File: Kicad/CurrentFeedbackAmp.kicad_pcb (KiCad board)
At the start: 2 copper layers, 200 x 100 mm, 123 parts, among them J1 Test_Etapa_3_Inf, J10 Protecc_Sup_In1, J11 Protecc_Inf_In1, J12 Protecc_Sup_In2, J13 Test_Etapa_3_Inf, J14 Entrada, J15 Salida masa2, J16 Salida tierra, J17 Salida senal, J2 Test_Realim_Out, J3 Salida masa1, J4 Protecc_Sup_Out, J5 Protecc_Inf_Out, J6 Conector Vcc, J7 Conector Vdd, J8 Test_Etapa_3_Inf, J9 Test_Etapa_3_Sup, Q1 TIP42C, Q10 BC858, Q11 BC848, Q12 BC858, Q13 BC559, Q14 BC559, Q15 BC559, Q16 BC549, Q17 BC549, Q18 BC549, Q19 BC559, Q2 BD135, Q20 BC549, Q21 BC559, Q22 BC549, Q23 BC848, Q24 BD136, Q25 BC858, Q26 BC848, Q27 BC848, Q28 BC848, Q29 BC858, Q3 BD136, Q30 BC858, Q31 BC848, Q32 BC858, Q33 BD135, Q34 TIP41C, Q35 BC858, Q36 BC848, Q37 BC848, Q38 BC848, Q4 BC848, Q40 BC858, Q41 BC858, Q5 BC848, Q6 BC858, Q7 BC858, Q8 BC848, Q9 BC858, U1 LM7812_TO220, U2 TL082, U3 LM7912_TO220, U4 LM7805_TO220, U5 LM7905_TO220

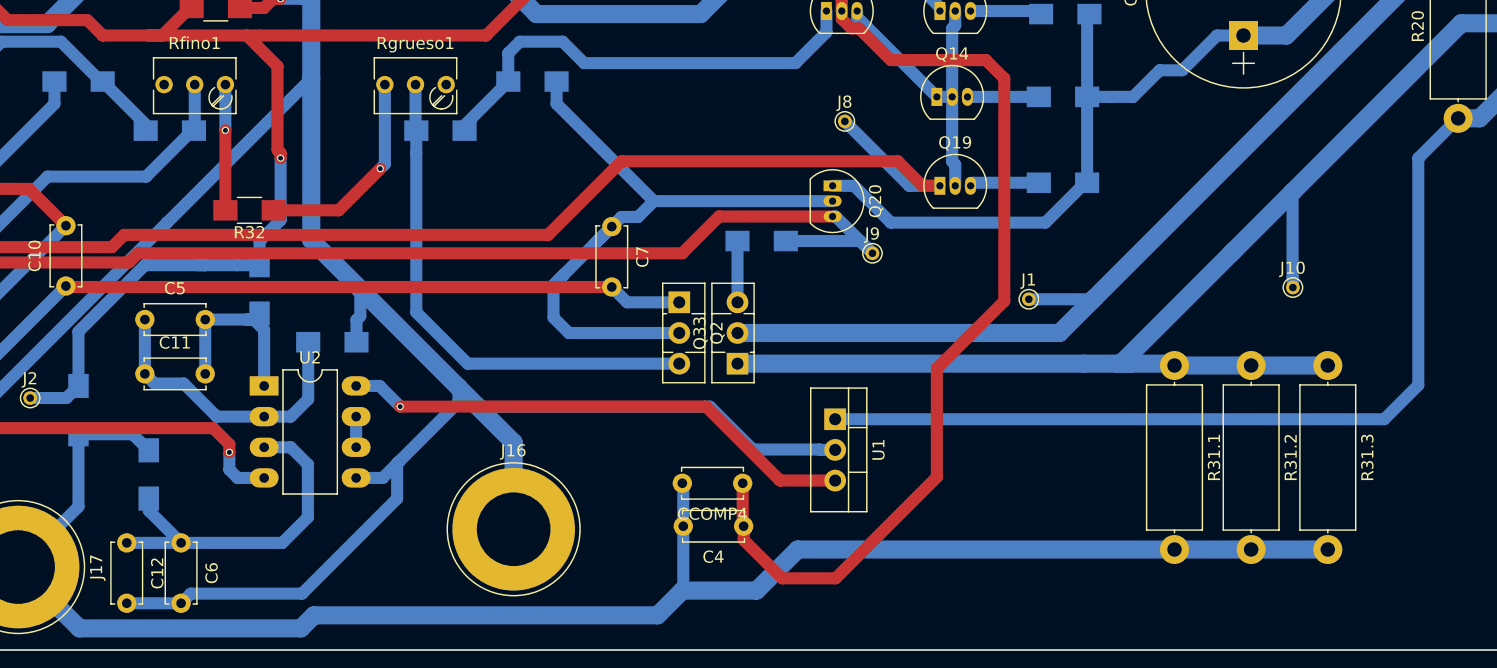
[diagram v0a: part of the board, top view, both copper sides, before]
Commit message: mover capacitores de SlewRate
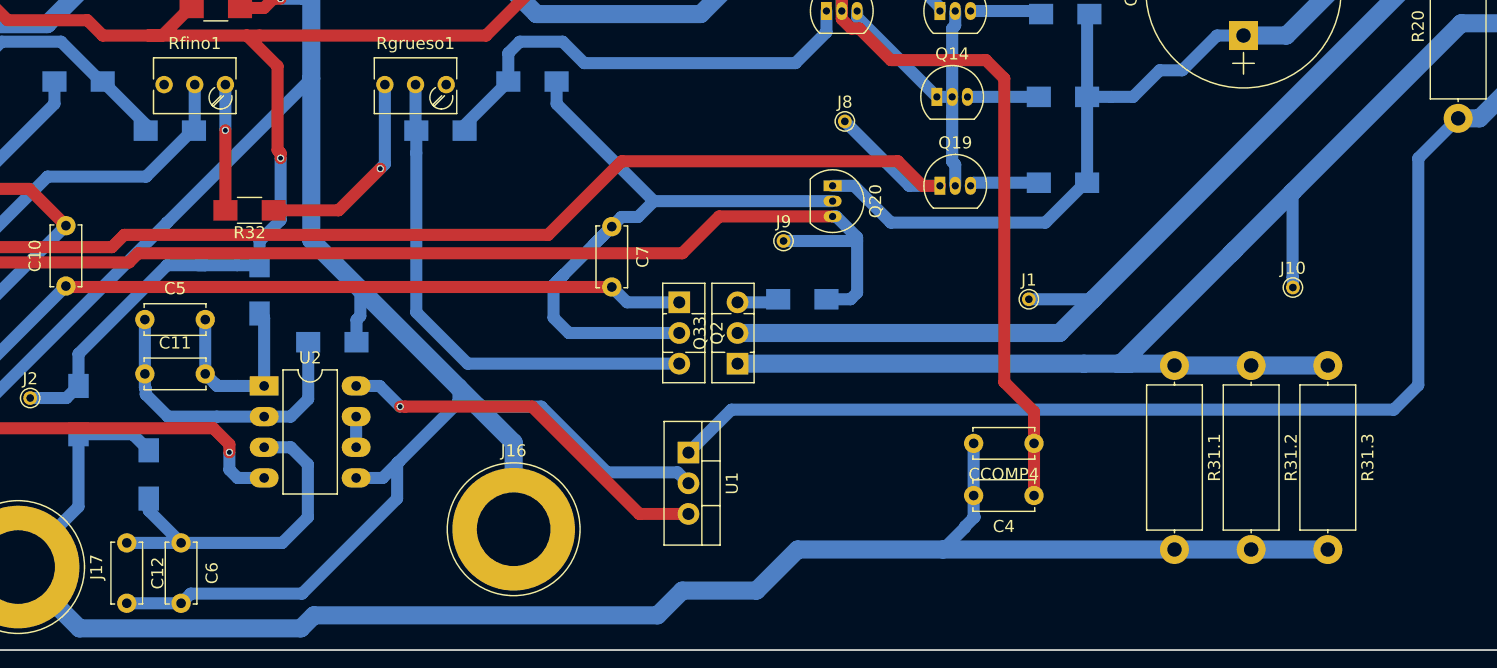
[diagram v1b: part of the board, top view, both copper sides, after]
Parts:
- moved CCOMP4 24.4 mm to (157.1, 95.8)
- moved C4 24.2 mm to (157.1, 100.1)
- moved U1 12.5 mm to (128.5, 96.5)
- moved J9 7.44 mm to (136.4, 79.0)
- moved R16 5.88 mm to (138.0, 83.8)
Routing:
- net Net-(C4-Pad1): track 123.2 -> 97.8 mm
- net Vcc: track 222.7 -> 236.0 mm
- net GND: track 461.4 -> 450.4 mm
- net VccTL: track 42.9 -> 31.9 mm
- net Net-(J9-Pad1): track 108.6 -> 112.8 mm
- net Net-(Q33-Pad3): track 5.08 -> 3.47 mm
- net Vin-: track 123.4 -> 122.3 mm
- net Net-(C11-Pad2): track 14.9 -> 16.0 mm
- net Net-(C11-Pad1): track 24.8 -> 25.8 mm
- net Vout: track 188.8 -> 189.8 mm

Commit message: reparacion version vieja vs nueva de Kicad. Si van a hacer algo gratuito y libre por lo menos haganlo bien!
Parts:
- Q1, Q34: footprint TO_SOT_Packages_THT:TO-220_Vertical -> TerminalBlock:TerminalBlock_bornier-3_P5.08mm
- R32: footprint Resistors_SMD:R_1206_HandSoldering -> Resistor_THT:R_Axial_DIN0204_L3.6mm_D1.6mm_P7.62mm_Horizontal
- moved CCOMP4 24.4 mm to (133.0, 99.1)
- moved C4 24.2 mm to (133.1, 102.6)
- moved R21 16.9 mm to (15.9, 69.8)
- moved R32 13.7 mm to (100.3, 65.4)
- moved J13 12.5 mm to (19.1, 92.1)
- moved U1 12.5 mm to (140.7, 93.8)
- moved J9 7.44 mm to (143.8, 80.0)
- moved R16 5.88 mm to (134.6, 79.0)
- moved Q1 3.42 mm to (198.1, 55.2)
- moved Q34 2.01 mm to (8.26, 62.9)
- moved J11 1.71 mm to (24.8, 74.9)
- moved R20 1.14 mm to (191.1, 68.8)
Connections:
- Rfino1 pad 3: (no net) -> Net-(Rfino1-Pad3)
- Rgrueso1 pad 1: (no net) -> Net-(Rgrueso1-Pad1)
- Rref3 pad 3: (no net) -> Net-(Rref3-Pad3)
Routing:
- net Net-(C4-Pad1): track 97.8 -> 123.2 mm
- net Net-(R32-Pad1): track 17.4 -> 3.31 mm, vias 1 -> 0
- net Net-(J13-Pad1): track 71.2 -> 85.0 mm
- net Vcc: track 236.0 -> 222.2 mm
- net Vdd: track 171.6 -> 184.1 mm
- net GND: track 450.4 -> 461.4 mm
- net VccTL: track 31.9 -> 42.9 mm
- net Net-(J11-Pad1): track 69.5 -> 79.3 mm
- net Net-(R32-Pad2): track 10.4 -> 2.80 mm, vias 1 -> 0
- net Net-(J9-Pad1): track 112.8 -> 108.6 mm
- net Net-(J1-Pad1): track 87.8 -> 85.9 mm
- net Net-(Q33-Pad3): track 3.47 -> 5.08 mm
- net Vin-: track 122.3 -> 121.3 mm
- net Net-(C11-Pad2): track 16.0 -> 14.9 mm
- net Net-(J10-Pad1): track 104.8 -> 103.8 mm
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
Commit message: Reestructuracion total, fede mode
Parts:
- R10, R15, R8, R9: moved to B.Cu
- moved C4 138.1 mm to (237.0, 11.7)
- moved CCOMP4 138.1 mm to (236.9, 8.13)
- moved R20 107.9 mm to (129.5, 157.5)
- moved J6 96.8 mm to (283.0, 18.5)
- moved Q1 96.8 mm to (294.9, 52.6)
- moved J7 94.5 mm to (-72.9, 4.06)
- moved J8 90.7 mm to (232.2, 67.6)
- moved J9 89.0 mm to (229.6, 56.4)
- moved Q34 88.9 mm to (-75.2, 93.5)
- moved C13 87.9 mm to (260.9, 78.4)
- moved C14 78.9 mm to (-52.8, 47.2)
- moved J12 78.5 mm to (-24.9, 100.3)
- moved J1 74.3 mm to (230.9, 87.4)
- moved J10 67.2 mm to (243.1, 101.6)
- moved C3 66.9 mm to (-9.40, 82.8)
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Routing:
- net GND: track 461.4 -> 109.4 mm, vias 1 -> 0
- net Vout: track 188.8 -> 3.59 mm
- net Vcc: track 222.2 -> 42.0 mm
- net Vdd: track 184.1 -> 14.8 mm
- net Net-(J9-Pad1): track 108.6 -> 0.00 mm
- net Net-(J8-Pad1): track 108.9 -> 2.54 mm
- net Net-(J10-Pad1): track 103.8 -> 0.22 mm
- net Vin-: track 121.3 -> 33.9 mm, vias 1 -> 0
- net Net-(J1-Pad1): track 85.9 -> 0.00 mm
- net Net-(J13-Pad1): track 85.0 -> 0.00 mm
- net Net-(J11-Pad1): track 79.3 -> 0.72 mm
- net Net-(C10-Pad1): track 64.3 -> 0.00 mm
- net Net-(C10-Pad2): track 58.4 -> 0.00 mm
- net Net-(C7-Pad1): track 55.8 -> 0.00 mm
- net Net-(Q23-Pad1): track 122.3 -> 69.6 mm
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
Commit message: ya esta colocado los potes de VBE mejoramos posicion de realimentacion
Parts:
- Q20, Q21: footprint TO_SOT_Packages_THT:TO-92_Inline_Narrow_Oval -> TO_SOT_Packages_THT:TO-126_Vertical
- R14, R25: footprint Resistors_THT:R_Axial_DIN0204_L3.6mm_D1.6mm_P7.62mm_Horizontal -> Resistors_SMD:R_1206_HandSoldering; moved to B.Cu
- moved U1 232.8 mm to (345.9, 72.4)
- moved Q24 150.2 mm to (-111.0, 43.7)
- moved Q3 150.2 mm to (-106.2, 48.8)
- moved R17 150.2 mm to (-94.3, 45.0)
- moved Q21 149.2 mm to (-106.2, 40.4), turned to 90 degrees
- moved U3 88.4 mm to (-10.7, 49.3)
- moved J2 46.8 mm to (69.8, 61.0)
- moved Q20 30.6 mm to (130.0, 71.4)
- moved C14 30.3 mm to (-72.4, 24.1)
- moved J7 30.0 mm to (-94.0, 25.4)
- moved Q33 27.1 mm to (134.6, 84.8)
- moved R16 26.8 mm to (140.5, 79.2)
- moved Q2 26.8 mm to (130.0, 79.8)
- moved R30 26.3 mm to (134.1, 66.0)
- moved R31 25.4 mm to (55.1, 66.0)
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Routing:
- net Net-(Q23-Pad1): track 69.6 -> 117.9 mm
- net Net-(Q15-Pad1): track 15.3 -> 60.1 mm
- net Net-(Q18-Pad1): track 15.3 -> 50.8 mm
- net Vout: track 3.59 -> 20.7 mm
- net VddTL: track 33.3 -> 16.5 mm
- net Net-(Q2-Pad3): track 3.84 -> 15.8 mm
- net Net-(Q3-Pad3): track 4.24 -> 15.3 mm
- net Vin-: track 33.9 -> 42.3 mm
- net GND: track 109.4 -> 101.8 mm
- net Vcc5: track 73.9 -> 80.4 mm
- net Ireference2: track 140.2 -> 134.9 mm, vias 3 -> 2
- net Net-(Q41-Pad3): track 5.34 -> 10.0 mm
- net VccTL: track 6.47 -> 2.81 mm
- net Ireference1: track 153.4 -> 156.7 mm
- net Vdd5: track 77.6 -> 80.2 mm
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
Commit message: va la primera version con Kicad 5
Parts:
- R16, R17: footprint Resistors_SMD:R_1206_HandSoldering -> Resistors_THT:R_Axial_DIN0204_L3.6mm_D1.6mm_P7.62mm_Horizontal
- moved Q3 162.4 mm to (52.1, 85.1)
- moved Q24 162.1 mm to (47.0, 80.0)
- moved Q21 156.0 mm to (47.0, 69.8), turned to 270 degrees
- moved R17 143.2 mm to (43.2, 85.1), turned to 90 degrees
- moved U1 134.7 mm to (214.6, 42.5)
- moved Q1 130.6 mm to (173.4, 100.3), turned to 180 degrees
- moved J7 119.0 mm to (11.4, 80.6)
- moved Q34 116.4 mm to (40.6, 105.4), turned to 180 degrees
- moved C14 113.8 mm to (18.4, 92.7), turned to 270 degrees
- moved J6 107.2 mm to (195.6, 80.6)
- moved C13 73.3 mm to (191.1, 101.0)
- moved J17 68.2 mm to (96.5, 94.0)
- moved R32.2 66.3 mm to (73.9, 96.6), turned to 180 degrees
- moved R32.1 65.1 mm to (73.9, 109.3), turned to 180 degrees
- moved R32.3 65.1 mm to (73.9, 103.0), turned to 180 degrees
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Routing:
- net Vcc: track 42.0 -> 183.9 mm
- net Vout: track 20.7 -> 103.7 mm
- net Net-(J11-Pad1): track 0.72 -> 74.4 mm
- net Vdd: track 13.5 -> 84.5 mm
- net Net-(J10-Pad1): track 0.22 -> 60.0 mm
- net Net-(C7-Pad1): track 0.00 -> 49.5 mm
- net Net-(J1-Pad1): track 0.00 -> 44.4 mm
- net Net-(Q2-Pad3): track 15.8 -> 55.9 mm
- net Net-(J13-Pad1): track 0.00 -> 35.0 mm
- net Net-(C10-Pad2): track 0.00 -> 32.1 mm
- net Net-(Q3-Pad3): track 15.3 -> 45.8 mm
- net Net-(C10-Pad1): track 0.00 -> 19.5 mm
- net Net-(Q33-Pad3): track 0.00 -> 10.6 mm
- net Net-(J9-Pad1): track 0.00 -> 10.2 mm
- net Net-(J8-Pad1): track 2.54 -> 8.15 mm
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
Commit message: Etapa de potencia, distancia minima entre pistas
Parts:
- moved J8 183.8 mm to (48.9, 81.9)
- moved C4 134.0 mm to (116.3, 70.1)
- moved CCOMP4 134.0 mm to (116.3, 66.5)
- moved J10 120.7 mm to (122.6, 108.6)
- moved J13 109.3 mm to (71.1, 108.6)
- moved C8 104.2 mm to (164.5, 102.2), turned to 90 degrees
- moved J12 101.6 mm to (76.2, 90.2)
- moved C3 91.2 mm to (80.1, 65.7)
- moved CCOMP3 91.2 mm to (80.1, 62.1)
- moved C9 84.5 mm to (26.7, 97.2), turned to 270 degrees
- moved J1 83.6 mm to (147.3, 87.4)
- moved J9 76.6 mm to (156.2, 78.1)
- moved J11 75.9 mm to (48.9, 92.1)
- moved C13 38.2 mm to (153.0, 103.5)
- moved R20 35.2 mm to (125.7, 83.8), turned to 0 degrees
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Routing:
- net Net-(J9-Pad1): track 10.2 -> 154.3 mm
- net Net-(J8-Pad1): track 8.15 -> 149.2 mm
- net Vdd: track 84.5 -> 203.5 mm
- net VccTL: track 2.81 -> 117.4 mm, vias 0 -> 1
- net VddTL: track 16.5 -> 116.8 mm, vias 0 -> 1
- net GND: track 101.8 -> 198.4 mm
- net Vout: track 103.7 -> 199.1 mm
- net Vin-: track 42.3 -> 127.0 mm
- net Vcc: track 183.9 -> 258.9 mm
- net Net-(C10-Pad1): track 19.5 -> 90.6 mm
- net Net-(Q2-Pad3): track 55.9 -> 32.2 mm
- net Net-(J11-Pad1): track 74.4 -> 51.0 mm
- net Net-(J10-Pad1): track 60.0 -> 39.4 mm
- net Net-(C7-Pad1): track 49.5 -> 29.5 mm
- net Net-(C4-Pad1): track 76.7 -> 91.9 mm
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
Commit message: Me falta solo conectar uno
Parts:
- Q10, Q11, Q12, Q23, Q25, Q26, Q27, Q28, Q29, Q30, Q31, Q32, Q35, Q36, Q37, Q38, Q4, Q40, Q41, Q5, Q6, Q7, Q8, Q9, R1, R11, R13, R14, R18, R2, R25, R26, R27, R28, R29, R6: moved to F.Cu
- moved R6 34.7 mm to (72.4, 38.8)
- moved J10 30.2 mm to (130.2, 79.4)
- moved R2 27.6 mm to (132.2, 57.8)
- moved Q9 26.9 mm to (66.3, 36.8), turned to 0 degrees
- moved Q8 26.5 mm to (140.3, 56.8)
- moved R11 25.0 mm to (38.6, 28.6)
- moved Q30 18.8 mm to (42.2, 42.3)
- moved Q37 18.0 mm to (46.7, 22.2), turned to 180 degrees
- moved Q28 16.2 mm to (125.7, 33.3), turned to 270 degrees
- moved Q12 15.7 mm to (141.0, 44.5), turned to 90 degrees
- moved Q7 14.5 mm to (37.5, 46.4)
- moved R18 13.8 mm to (159.3, 34.3)
- moved Q11 12.7 mm to (52.7, 29.7), turned to 90 degrees
- moved Q6 12.2 mm to (45.7, 47.9), turned to 270 degrees
- moved Q23 11.9 mm to (56.9, 36.8), turned to 180 degrees
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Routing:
- net GND: track 198.4 -> 542.5 mm
- net Net-(Q23-Pad1): track 118.9 -> 0.00 mm, vias 2 -> 0
- net Ireference2: track 134.9 -> 93.4 mm, vias 2 -> 0
- net Vin+: track 152.0 -> 112.8 mm, vias 3 -> 5
- net Ireference1: track 153.4 -> 114.5 mm, vias 3 -> 2
- net Net-(Q37-Pad3): track 30.2 -> 5.08 mm
- net Vdd5: track 80.2 -> 55.9 mm
- net Net-(C4-Pad1): track 91.9 -> 115.7 mm, vias 0 -> 1
- net Vcc: track 258.9 -> 236.6 mm
- net Vcc5: track 80.4 -> 58.4 mm
- net Net-(Q12-Pad1): track 121.8 -> 100.2 mm, vias 2 -> 4
- net Vin-: track 127.0 -> 112.5 mm, vias 0 -> 2
- net Net-(Q29-Pad1): track 5.54 -> 18.0 mm
- net VddTL: track 116.8 -> 127.6 mm
- net Net-(J13-Pad1): track 34.6 -> 43.4 mm
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
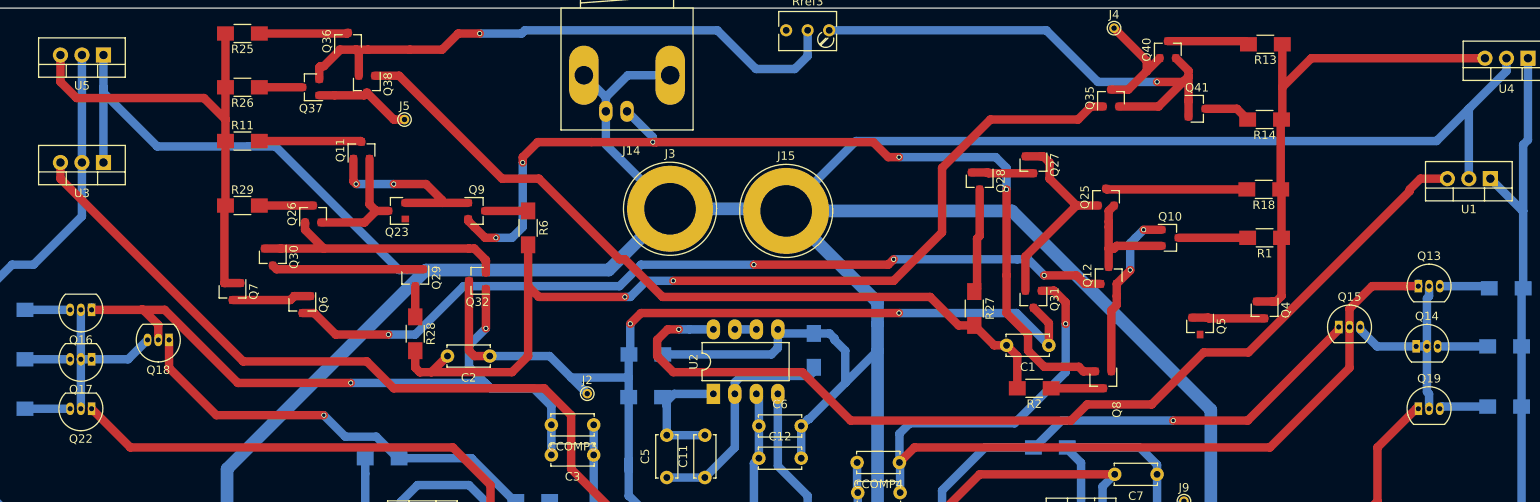
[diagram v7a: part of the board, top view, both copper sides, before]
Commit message: Modifique algunas conexiones en transistores para que la conexion en si entre pista y transitor sea en el back en vez del front, obviamente que para lograrlo tuve que agregar algunas vias mas
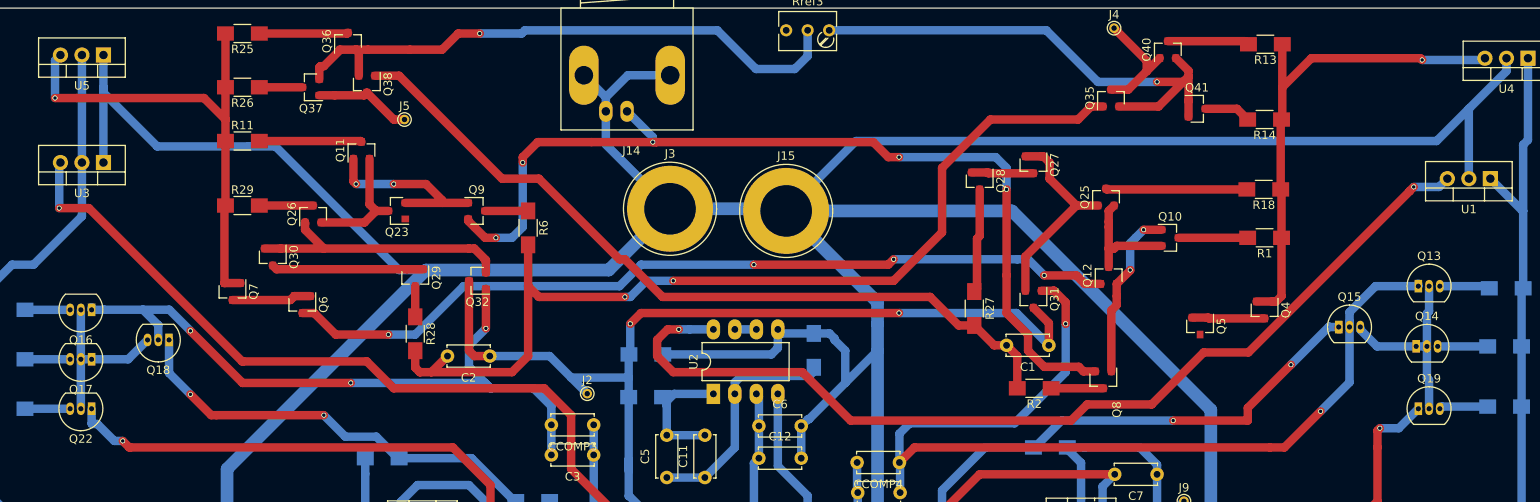
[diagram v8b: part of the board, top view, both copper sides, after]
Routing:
- net VddTL: track 127.6 -> 129.8 mm, vias 1 -> 2
- net Vdd5: track 55.9 -> 58.0 mm, vias 0 -> 1
- net Net-(C4-Pad1): track 115.7 -> 117.2 mm, vias 1 -> 2
- net Net-(J8-Pad1): track 148.3 -> 149.5 mm, vias 0 -> 1
- net Net-(Q15-Pad1): track 58.3 -> 59.4 mm, vias 1 -> 2
- net Net-(J9-Pad1): track 151.6 -> 152.6 mm, vias 0 -> 1
- net Net-(Q18-Pad1): track 50.8 -> 51.1 mm, vias 1 -> 2
- net Net-(C3-Pad2): track 83.3 -> 83.1 mm, vias 2 -> 3
- net Vcc5: track 58.4 -> 58.6 mm, vias 0 -> 1
- net VccTL: track 117.5 -> 117.4 mm, vias 1 -> 2
